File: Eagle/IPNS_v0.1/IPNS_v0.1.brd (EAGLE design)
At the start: 32.7 x 33 mm, 30 parts, among them Q1 16MHz, Q2 32.768 kHz, U1 STM8L152C4_C6TX

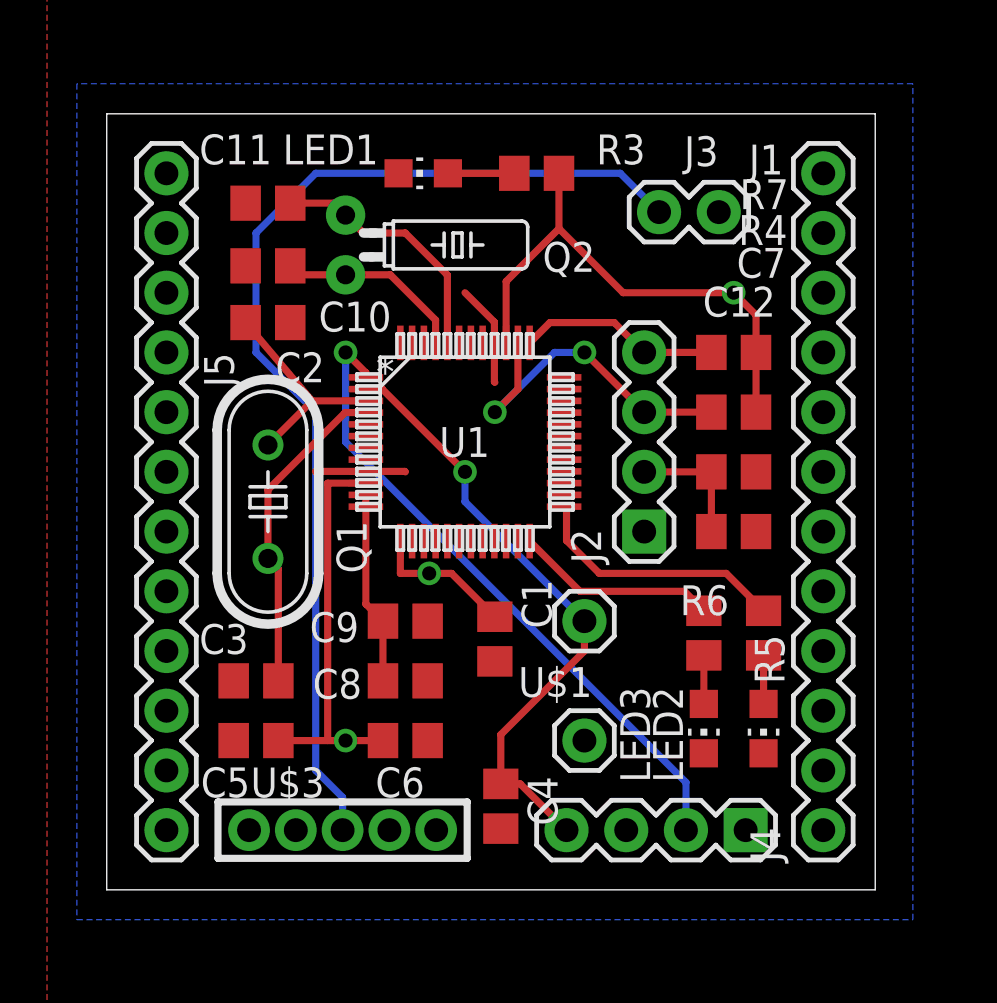
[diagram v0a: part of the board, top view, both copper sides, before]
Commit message: Routed Vbatt, Vmcu (3.3V), GND, and PWM and DAC to breakout pins
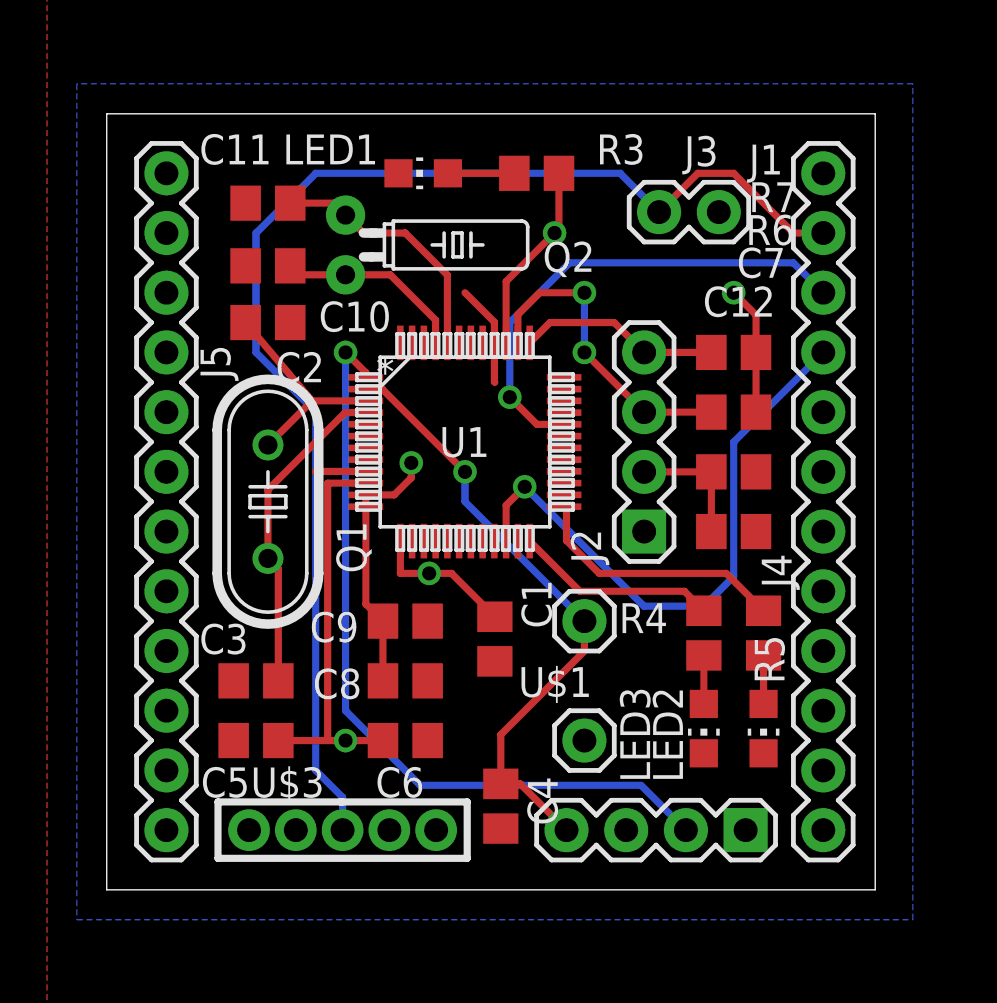
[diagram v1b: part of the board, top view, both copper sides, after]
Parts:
- J1: value (none) -> SWIM
- J2: value (none) -> NFC
- J3: value (none) -> BATT
- J4: value (none) -> LEFT CONN
- J5: value (none) -> RIGHT CONN
- R3: value (none) -> 220
- R4: value (none) -> 330
- R5: value (none) -> 660
- R6, R7: value (none) -> 1k
- moved J4 27.9 mm to (30.5, 30.5), turned to 270 degrees
- moved J5 27.9 mm to (2.54, 30.5), turned to 270 degrees
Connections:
- removed net OFF: U$3.2
- removed net PULSE: U1.22
- new net PWM: J4.4, U1.22
- net +3V3: now also J5.2
- net DAC: now also J4.3
- net GND: now also J4.1, J4.12, J5.1, J5.12
- net VBATT: now also J4.2
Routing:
- net PWM: track 0.00 -> 25.3 mm, vias 0 -> 1
- net DAC: track 0.00 -> 20.9 mm, vias 0 -> 1
- net VBATT: track 45.8 -> 54.5 mm
- net +3V3: track 59.0 -> 53.3 mm, vias 3 -> 5
- net ST_LINK_SWIM: track 27.7 -> 33.2 mm
- net GND: track 8.17 -> 6.49 mm
- net SCL: track 14.7 -> 13.4 mm
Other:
- board text added: "Alexey Revinski"
- board text added: "IPNS_v0.1"
- board text added: "NU BME 390"
